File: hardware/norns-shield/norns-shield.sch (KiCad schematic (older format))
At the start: 48 parts, among them J1 Audio In, J2 Audio Out, SW1 SW_DPST, SW2 SW_DPST, SW3 SW_DPST, U1 CS4270, U2 OLED128x64, X1 Pi Model B GPIO Port

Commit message: Almost done with schematic
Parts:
- added C10, C12: 10u, symbol Device:C_Small
- added C11, C13: 220p, symbol Device:C_Small
- added C14, C16: 3.3u, symbol Device:C_Small
- added C15, C17: 2700p, symbol Device:C_Small
- added J3: ISP-ROW, _isp-row:Harwin-M20-8890645-MFG, symbol norns_symbols:ISP-ROW
- added R10, R8: 1.5k, symbol Device:R_Small_US
- added R11, R13: 10k, symbol Device:R_Small_US
- added R12, R14: 470, symbol Device:R_Small_US
- added R7, R9: 3.3k, symbol Device:R_Small_US
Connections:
- net GND: now also J3.1 (VCC)
- net GNDA: now also J1.S, J2.S, C11.1, C13.1, C15.1, C17.1, R10.1, R11.1, R13.1, R8.1
- net INA: now also C10.1, C11.2
- net INB: now also C12.1, C13.2
- net OUTA: now also C14.1
- net OUTB: now also C16.1
- net R-CODEC: now also X1.11 (GPIO17)
- net SCLK: now also X1.12 (GPIO18/PWM0)
- net RX: now reaches X1.10 (GPIO15/RXD)
- net RX: now also J3.4 (SCK)
- net TX: now reaches X1.8 (GPIO14/TXD)
- net TX: now also J3.5 (RESET)
- net at J1.R: now also R9.2
- net at J1.T: now also R7.2
- net at J2.R: now also C17.2, R14.2
- net at J2.T: now also C15.2, R12.2
- new net: C10.2, R7.1, R8.2
- new net: C12.2, R10.2, R9.1
- new net: C14.2, R11.2, R12.1
- new net: C16.2, R13.2, R14.1
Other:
- note added: "Filtered Stereo Inputs/Outputs"
- note removed: "R-CODEC"
- note removed: "SCLK"
- moved on the sheet: J1, J2, R15, U1, X1

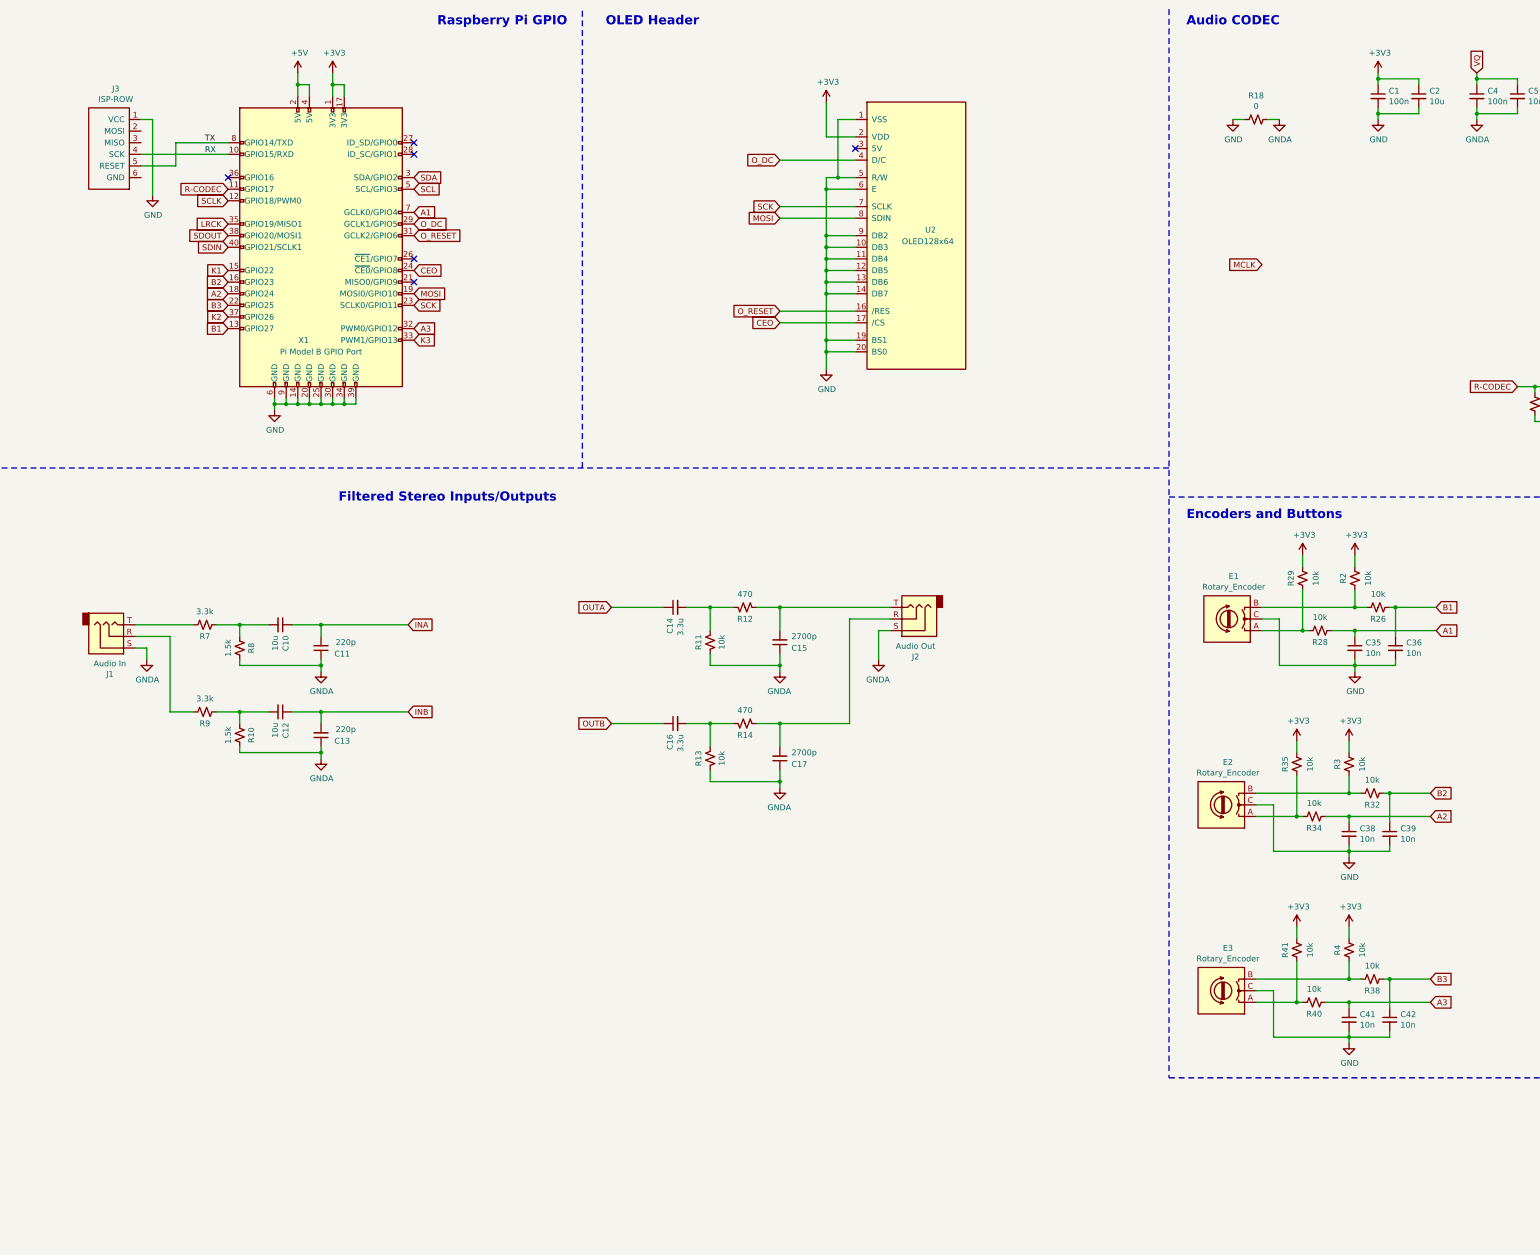
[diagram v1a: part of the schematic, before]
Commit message: Schem ready to be laid out
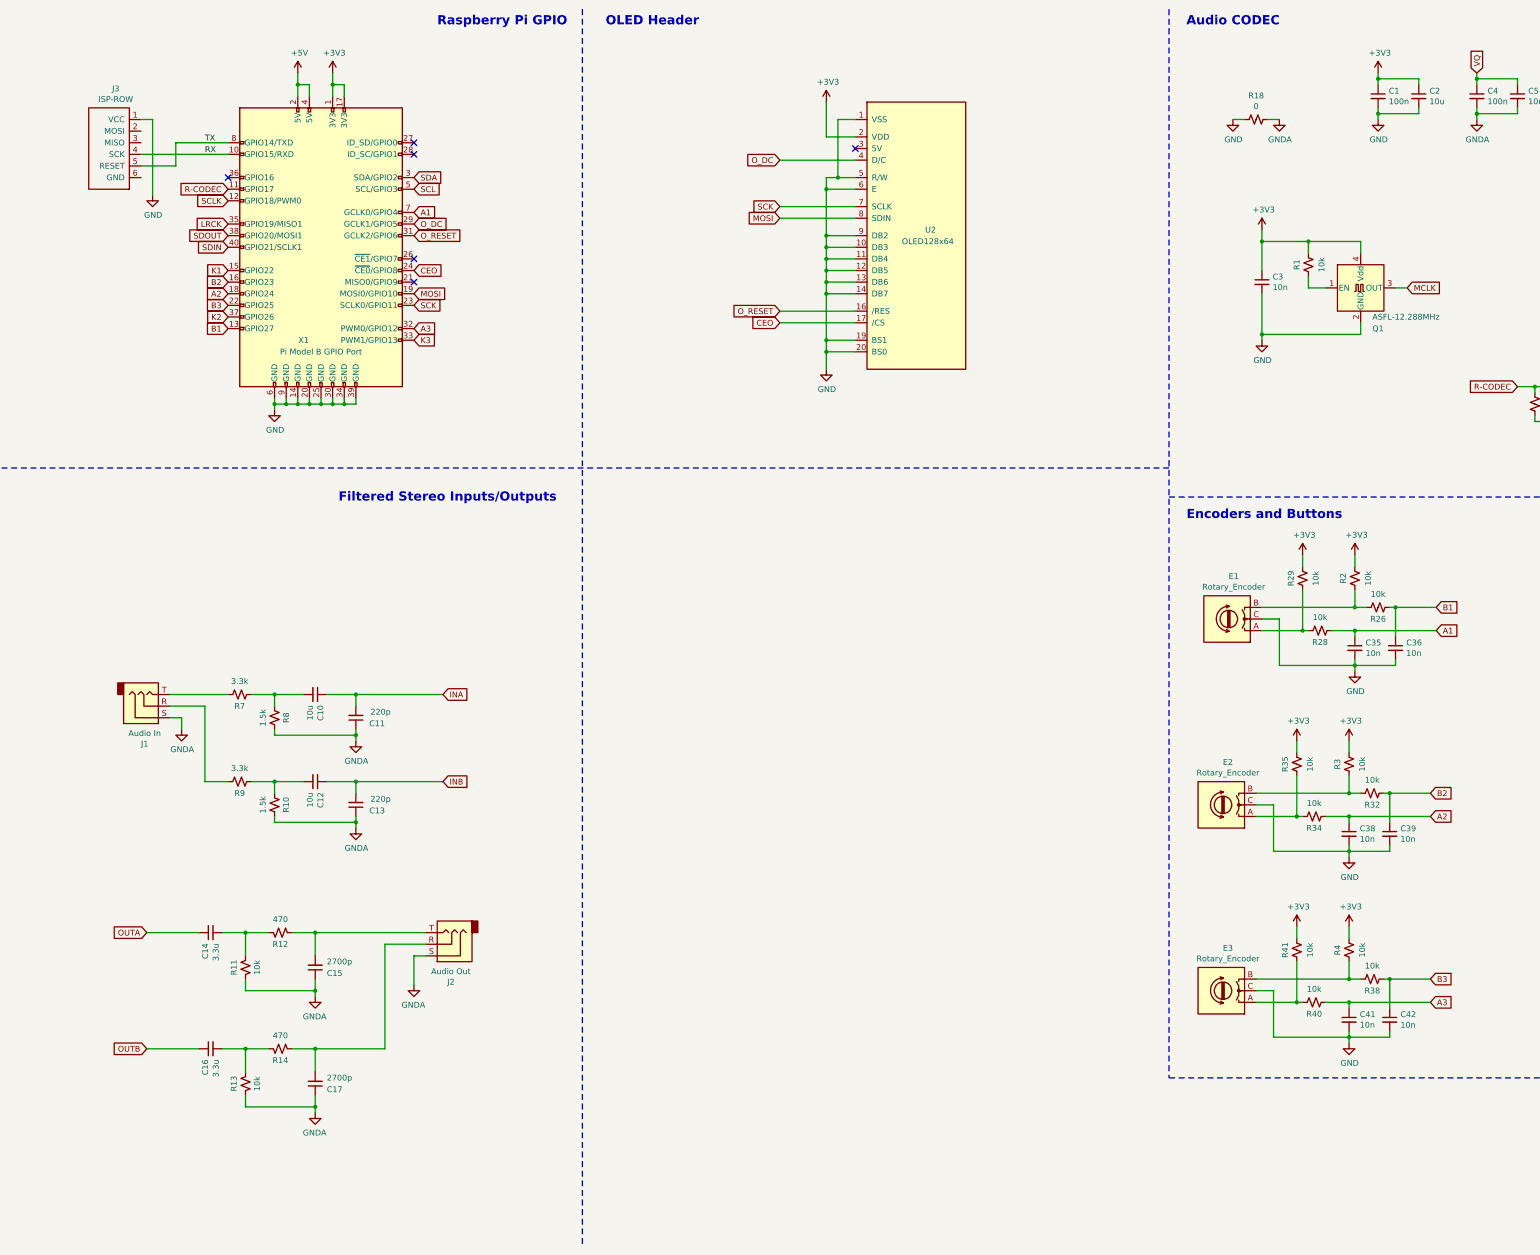
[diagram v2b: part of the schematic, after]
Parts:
- added C3: 10n, symbol Device:C_Small
- added Q1: ASFL-12.288MHz, Oscillator:Oscillator_SMD_Abracon_ASV-4Pin_7.0x5.1mm, symbol Oscillator:ASV-xxxMHz
- added R1: 10k, symbol Device:R_Small_US
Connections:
- net +3V3: now also C3.1, Q1.4 (Vdd), R1.2
- net GND: now also C3.2, Q1.2 (GND)
- net MCLK: now also Q1.3 (OUT)
- new net: Q1.1 (EN), R1.1
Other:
- moved on the sheet: C10, C11, C12, C13, C14, C15, C16, C17, J1, J2, R10, R11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
